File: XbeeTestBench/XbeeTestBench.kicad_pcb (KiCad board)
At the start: 2 copper layers, 76 x 61 mm, 10 parts, among them J1 Conn_01x02, J2 Conn_01x06, J3 Conn_01x15, J4 Conn_01x15, U1 Xbee802.15.4

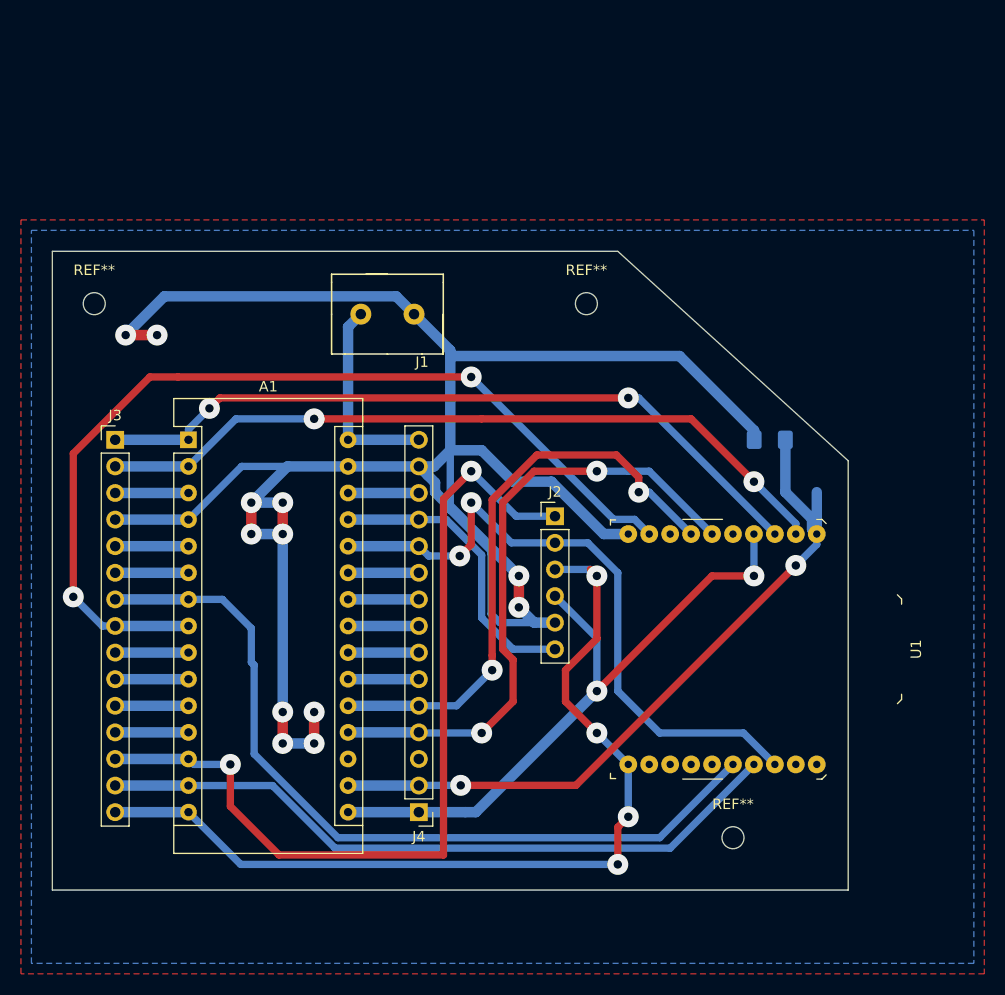
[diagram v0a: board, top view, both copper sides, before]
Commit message: Mise à jour + PDF Banc Xbee
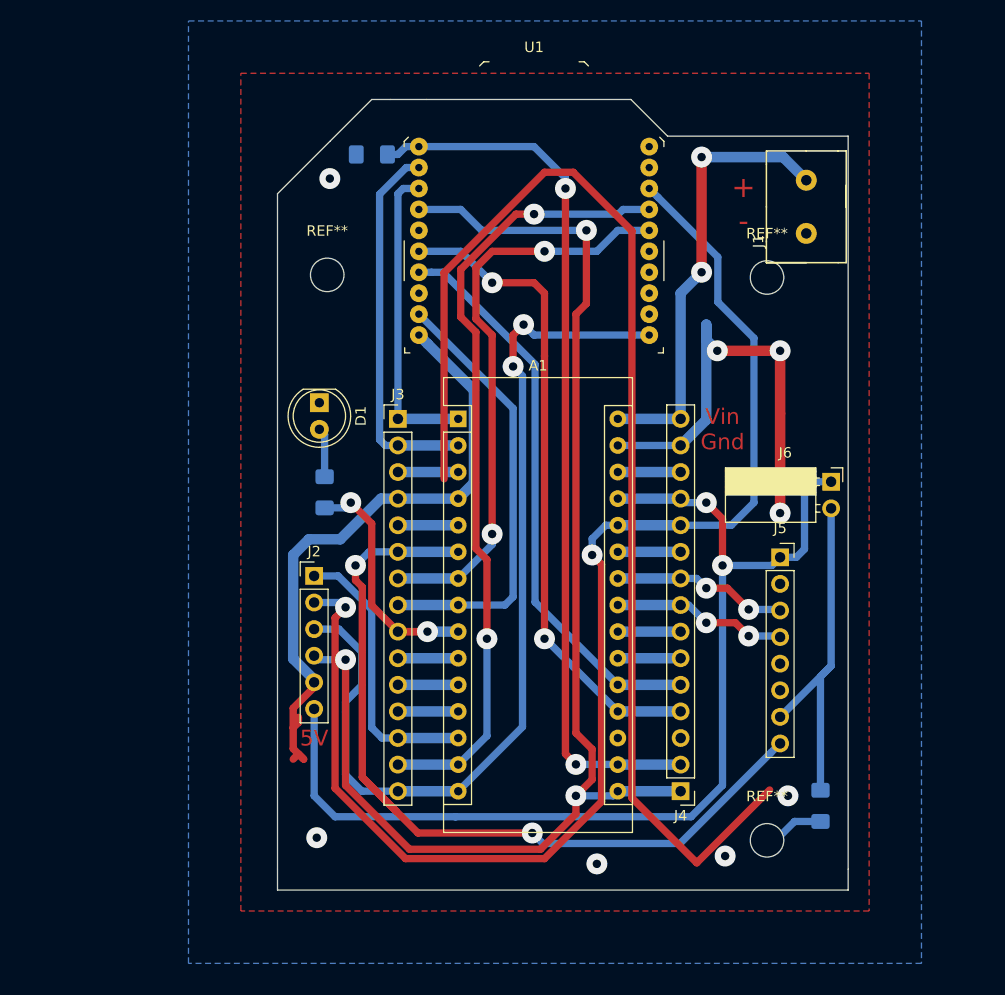
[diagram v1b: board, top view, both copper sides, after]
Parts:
- removed the REF** at (157.0, 98.0)
- removed the REF** at (96.0, 47.0)
- removed the REF** at (143.0, 47.0)
- added D1: LED, LED_THT:LED_D5.0mm, F.Cu at (117.5, 56.5)
- added J5: Conn_01x08, Connector_PinSocket_2.54mm:PinSocket_1x08_P2.54mm_Vertical, F.Cu at (161.5, 71.2)
- added J6: Conn_01x02, Connector_PinSocket_2.54mm:PinSocket_1x02_P2.54mm_Horizontal, F.Cu at (166.4, 64.0)
- added R1: 1kR_Led, Resistor_SMD:R_1206_3216Metric_Pad1.42x1.75mm_HandSolder, B.Cu at (118.0, 65.0)
- added R2: 1kR_ADPullDown, Resistor_SMD:R_1206_3216Metric_Pad1.42x1.75mm_HandSolder, B.Cu at (165.4, 95.0)
- added REF**: MountingHole_3.2mm_M3, MountingHole:MountingHole_3.2mm_M3, F.Cu at (118.2, 44.2)
- added REF**: MountingHole_3.2mm_M3, MountingHole:MountingHole_3.2mm_M3, F.Cu at (160.2, 98.2)
- added REF**: MountingHole_3.2mm_M3, MountingHole:MountingHole_3.2mm_M3, F.Cu at (160.2, 44.5)
- moved C1 46.8 mm to (122.5, 32.8)
- moved U1 43.0 mm to (138.0, 41.0), turned to 0 degrees
- moved J1 41.3 mm to (164.0, 37.8), turned to 90 degrees
- moved J3 27.1 mm to (125.0, 58.0)
- moved A1 25.8 mm to (130.8, 58.0)
- moved J4 25.1 mm to (152.0, 93.6)
- moved J2 23.7 mm to (117.0, 73.0)
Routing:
- net /6: track 7.00 -> 81.9 mm, vias 0 -> 2
- net +5V: track 28.4 -> 102.5 mm, vias 0 -> 2
- net /26: track 62.6 -> 127.9 mm
- net /16: track 62.8 -> 125.5 mm, vias 2 -> 3
- net /13: track 85.0 -> 26.8 mm, vias 2 -> 0
- net /8: track 90.1 -> 42.1 mm, vias 2 -> 0
- net /1: track 70.6 -> 29.5 mm, vias 2 -> 0
- net /2: track 72.0 -> 36.0 mm, vias 2 -> 0
- net /AD0: track 0.00 -> 34.2 mm
- net /30: track 19.3 -> 42.7 mm, vias 0 -> 2
- net /7: track 78.2 -> 55.5 mm, vias 0 -> 2
- net /9: track 7.00 -> 25.0 mm, vias 0 -> 2
- net VCC: track 69.5 -> 85.0 mm
- net /24: track 6.76 -> 16.8 mm, vias 0 -> 2
- net /23: track 6.76 -> 16.8 mm, vias 0 -> 2
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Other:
- board size 76 x 61 mm -> 54.5 x 75.5 mm
- board text added: "+ -"
- board text added: "5V"
- board text added: "Vin Gnd"

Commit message: MàJ des test bench, ajout des projets ElecExterne et ElecInterne
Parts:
- removed REF** (x3): MountingHole_3.2mm_M3, MountingHole:MountingHole_3.2mm_M3
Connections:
- J2 pad 5: GND -> +5V
- J2 pad 6: +5V -> GND
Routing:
- net GND: track 225.0 -> 208.7 mm, vias 8 -> 11
- net +5V: track 102.5 -> 110.1 mm
- net /6: track 81.9 -> 83.1 mm
